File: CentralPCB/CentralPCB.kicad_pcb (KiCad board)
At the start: 2 copper layers, 71.1 x 76.2 mm, 60 parts, among them J1 POWER HEADER, J2 SPI Header, J3 Conn_01x24, J4 Conn_01x24, J5 Conn_02x16_Odd_Even, J6 Conn_Coaxial, J7 Conn_02x10_Odd_Even, J8 Conn_01x05, U1 AD8531, U2 Teensy4.1, U3 BA7810CP-E2

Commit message: Finished CentralPCB
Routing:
- net GND: track 94.7 -> 103.7 mm, vias 19 -> 22
- net +5V: track 210.8 -> 213.4 mm
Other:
- board size 71.1 x 76.2 mm -> 71.1 x 78.7 mm
- rule via_min_drill: 0.254 -> 0.3
- rule via_min_size: 0.508 -> 0.6
- board text added: "+12V"
- board text added: "+5V"
- board text added: "-12V"
- board text added: "12V"
- board text added: "3.3V"
- board text added: "5V"
- board text added: "AGND"
- board text added: "CS"
- board text added: "DAC POW"
- board text added: "DAC REF"
- board text added: "DAC SIG"
- board text added: "DGND"
- board text added: "DIN"
- board text added: "DVCC"
- board text added: "GND"
- board text added: "GND->"
- board text added: "MISO"
- board text added: "MOSI"
- board text added: "MREC"
- board text added: "MTRA"
- board text added: "SCK"
- board text added: "SCL"
- board text added: "SCLK"
- board text added: "SDA"
- board text added: "SPI"
- board text added: "VDD"
- board text added: "VSS"

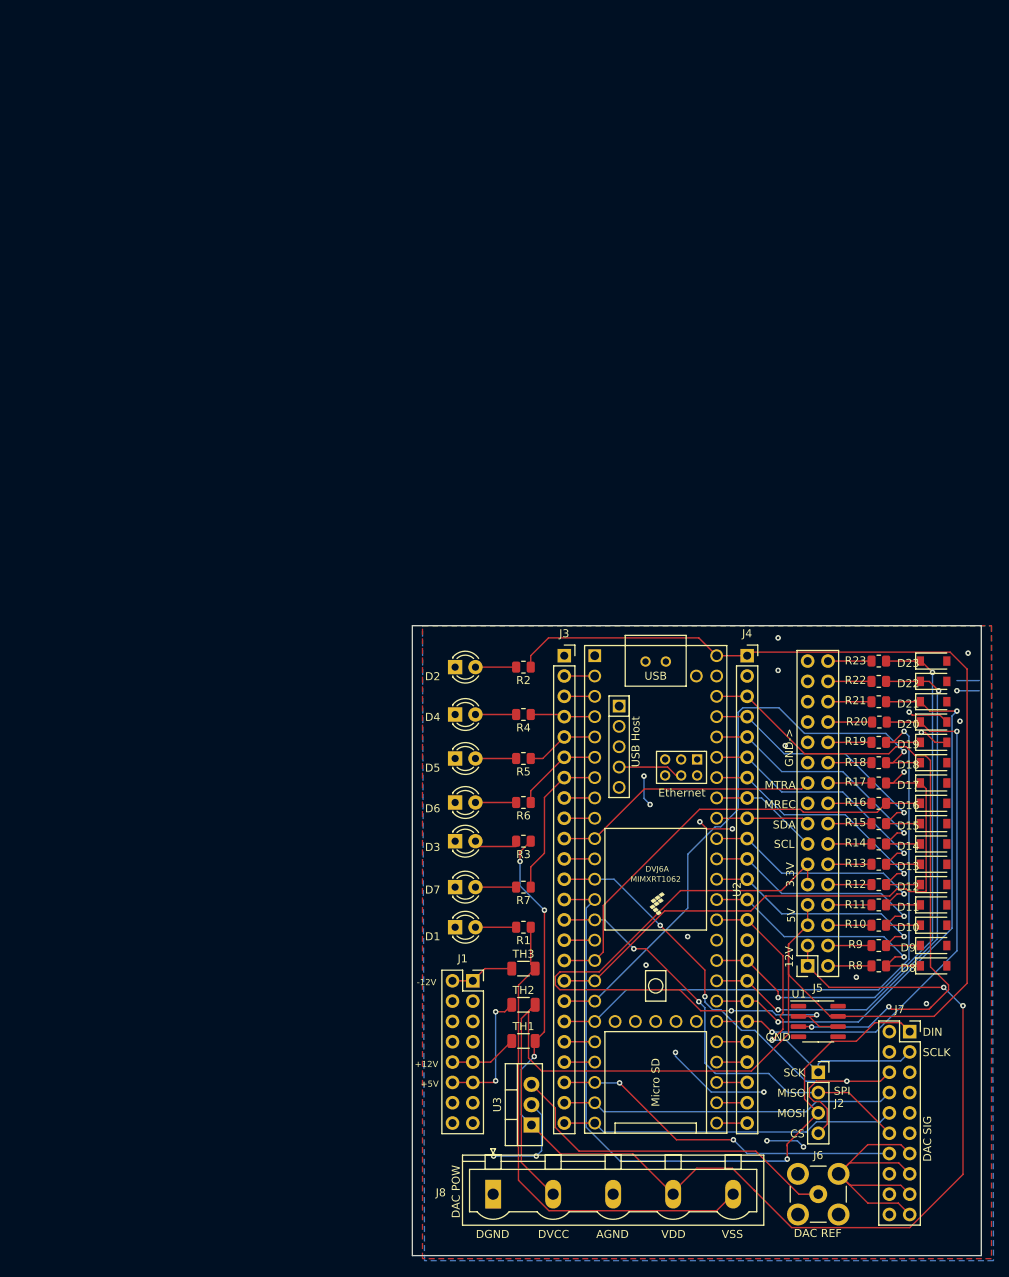
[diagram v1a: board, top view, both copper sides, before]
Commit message: Added additional protection for CentralPCB
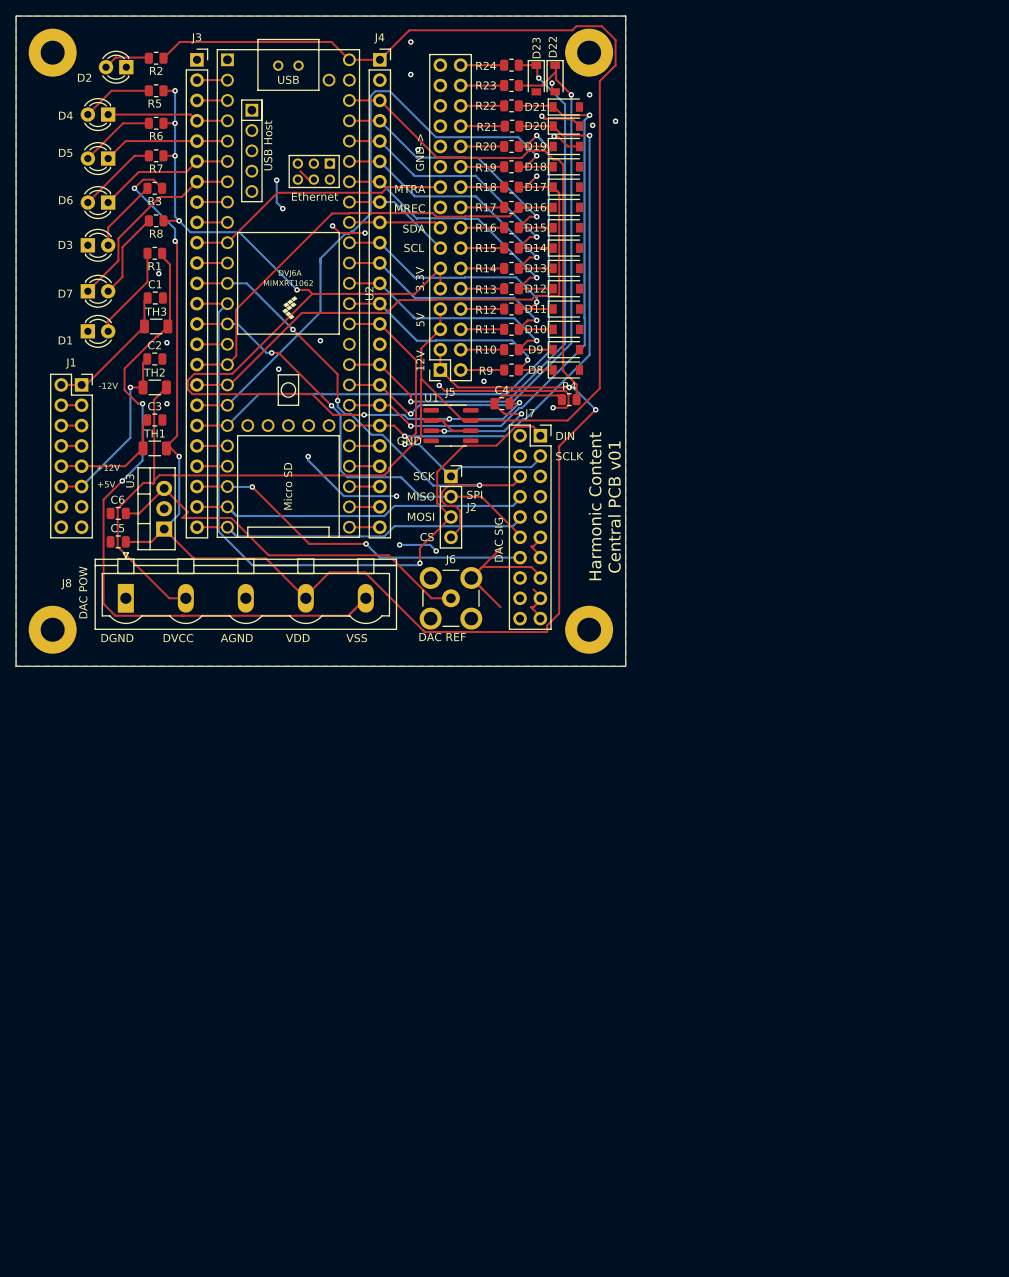
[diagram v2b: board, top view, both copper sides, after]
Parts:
- added  : MountingHole_3mm_Pad, MountingHole:MountingHole_3mm_Pad, F.Cu at (97.0, 102.1)
- added  : MountingHole_3mm_Pad, MountingHole:MountingHole_3mm_Pad, F.Cu at (30.0, 102.1)
- added  : MountingHole_3mm_Pad, MountingHole:MountingHole_3mm_Pad, F.Cu at (30.0, 30.0)
- added  : MountingHole_3mm_Pad, MountingHole:MountingHole_3mm_Pad, F.Cu at (97.0, 30.0)
- added C1: .1u, Capacitor_SMD:C_0805_2012Metric, F.Cu at (42.8, 60.6)
- added C2: .1u, Capacitor_SMD:C_0805_2012Metric, F.Cu at (42.7, 68.3)
- added C3: .1u, Capacitor_SMD:C_0805_2012Metric, F.Cu at (42.7, 75.9)
- added C4: .1u, Capacitor_SMD:C_0805_2012Metric, F.Cu at (86.1, 73.9)
- added C5: .33u, Capacitor_SMD:C_0805_2012Metric, F.Cu at (38.2, 91.1)
- added C6: .1u, Capacitor_SMD:C_0805_2012Metric, F.Cu at (38.2, 87.6)
- added R4: 10k, Resistor_SMD:R_0805_2012Metric, F.Cu at (94.6, 73.3)
- moved R1 96.0 mm to (42.7, 55.1)
- moved R8 95.1 mm to (42.9, 51.0)
- moved R3 93.7 mm to (42.7, 46.9)
- moved R7 93.0 mm to (42.9, 42.9)
- moved TH3 92.5 mm to (42.9, 64.2)
- moved R6 91.7 mm to (42.9, 38.8)
- moved R5 90.5 mm to (42.9, 34.7)
- moved TH2 89.9 mm to (42.7, 71.8)
- moved J1 89.1 mm to (33.6, 71.5)
- moved D22 89.0 mm to (92.8, 33.2), turned to 270 degrees
- moved R2 88.9 mm to (42.9, 30.7)
- moved D23 88.1 mm to (90.4, 33.2), turned to 270 degrees
- moved J7 87.6 mm to (90.9, 77.9)
- moved D10 87.5 mm to (94.2, 64.6)
- moved D11 87.5 mm to (94.2, 62.0)
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- renumbered R9 to R10, R10 to R11, R11 to R12, R12 to R13, R13 to R14, R14 to R15, R15 to R16, R16 to R17, R17 to R18, R18 to R19, R19 to R20, R20 to R21, R21 to R22, R22 to R23, R23 to R24, R4 to R5, R5 to R6, R6 to R7, R7 to R8, R8 to R9
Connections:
- D4 pad 1: GND -> Net-(D4-Pad1)
- D5 pad 1: GND -> Net-(D5-Pad1)
- D6 pad 1: GND -> Net-(D6-Pad1)
- D7 pad 1: GND -> Net-(D7-Pad1)
- J3 pad 4: Net-(J3-Pad4) -> Net-(D4-Pad1)
- J3 pad 5: Net-(J3-Pad5) -> Net-(D5-Pad1)
- J3 pad 6: Net-(J3-Pad6) -> Net-(D6-Pad1)
- J3 pad 7: Net-(J3-Pad7) -> Net-(D7-Pad1)
- R5 pad 1: Net-(J3-Pad4) -> +3V3
- R6 pad 1: Net-(J3-Pad5) -> +3V3
- R7 pad 1: Net-(J3-Pad6) -> +3V3
- R8 pad 1: Net-(J3-Pad7) -> +3V3
- U1 pad 3: Net-(J4-Pad3) -> Net-(C4-Pad1)
- U2 pad 4: Net-(J3-Pad4) -> Net-(D4-Pad1)
- U2 pad 5: Net-(J3-Pad5) -> Net-(D5-Pad1)
- U2 pad 6: Net-(J3-Pad6) -> Net-(D6-Pad1)
- U2 pad 7: Net-(J3-Pad7) -> Net-(D7-Pad1)
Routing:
- net +3V3: track 83.0 -> 137.4 mm, vias 2 -> 8
- net Net-(C4-Pad1): track 0.00 -> 25.5 mm, vias 0 -> 2
- net -12V: track 62.0 -> 87.5 mm, vias 0 -> 2
- net Net-(D7-Pad1): track 0.00 -> 24.7 mm
- net Net-(J4-Pad3): track 81.6 -> 60.9 mm, vias 2 -> 0
- net Net-(J3-Pad7): track 19.2 -> 0.00 mm
- net +12V: track 149.2 -> 167.8 mm
- net Net-(D6-Pad1): track 0.00 -> 17.0 mm
- net Net-(D5-Pad1): track 0.00 -> 15.8 mm
- net Net-(D4-Pad1): track 0.00 -> 15.6 mm
- net Net-(J3-Pad6): track 11.2 -> 0.00 mm
- net Net-(J3-Pad5): track 9.11 -> 0.00 mm
- net Net-(C1-Pad1): track 8.04 -> 17.1 mm
- net Net-(J3-Pad4): track 8.11 -> 0.00 mm
- net +5V: track 213.4 -> 220.7 mm
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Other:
- board size 71.1 x 78.7 mm -> 76.2 x 81.3 mm
- net class Default: trace_width 0.1778 -> 0.254
- rule trace_min: 0.1524 -> 0.254
- board text added: "Harmonic Content Central PCB v01"

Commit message: small silkscreen changes on centralpcb
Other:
- board text added: "Eurorack power"
- board text added: "Red Stripe"
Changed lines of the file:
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@@
-(kicad_pcb (version 20171130) (host pcbnew "(5.1.10)-1")
+(kicad_pcb (version 20171130) (host pcbnew "(5.1.4)-1")
   (general
     (thickness 1.6)
-    (drawings 34)
+    (drawings 36)
     (tracks 680)
     (zones 0)
@@
     )
   )
+  (gr_text "Eurorack power" (at 27.9 80.4 90) (layer F.SilkS)
+    (effects (font (size 1 1) (thickness 0.15)))
+  )
+  (gr_text "Red Stripe" (at 35.9 68.9) (layer F.SilkS)
+    (effects (font (size 0.508 0.508) (thickness 0.127)))
+  )
   (dimension 76.2 (width 0.15) (layer Dwgs.User)
     (gr_text "3.0000 in" (at 63.5 22.83) (layer Dwgs.User)
@@
   (segment (start 94.964799 38.289799) (end 93.788799 38.289799) (width 0.254) (layer F.Cu) (net 2))
   (segment (start 90.072799 97.057799) (end 91.1895 98.1745) (width 0.254) (layer F.Cu) (net 2))
+  (via (at 92.3925 33.782) (size 0.6858) (drill 0.3302) (layers F.Cu B.Cu) (net 2))
+  (segment (start 92.3925 34.4795) (end 92.7735 34.8605) (width 0.254) (layer F.Cu) (net 2))
+  (segment (start 92.3925 33.782) (end 92.3925 34.4795) (width 0.254) (layer F.Cu) (net 2))
   (via (at 90.7415 33.147) (size 0.6858) (drill 0.3302) (layers F.Cu B.Cu) (net 3))
   (via (at 74.7395 73.5965) (size 0.6858) (drill 0.3302) (layers F.Cu B.Cu) (net 3))
@@
   (segment (start 74.7395 73.5965) (end 86.758736 73.5965) (width 0.254) (layer B.Cu) (net 3))
   (segment (start 88.3606 31.6611) (end 88.236 31.5365) (width 0.254) (layer F.Cu) (net 3))
+  (segment (start 90.527 31.5365) (end 90.551 31.5605) (width 0.254) (layer F.Cu) (net 3))
+  (segment (start 88.236 31.5365) (end 90.527 31.5365) (width 0.254) (layer F.Cu) (net 3))
+  (segment (start 90.551 32.9565) (end 90.7415 33.147) (width 0.254) (layer F.Cu) (net 3))
+  (segment (start 90.551 31.5605) (end 90.551 32.9565) (width 0.254) (layer F.Cu) (net 3))
+  (segment (start 94.020618 36.426118) (end 94.020618 66.334618) (width 0.254) (layer B.Cu) (net 3))
+  (segment (start 90.7415 33.147) (end 94.020618 36.426118) (width 0.254) (layer B.Cu) (net 3))
   (via (at 94.8055 35.2425) (size 0.6858) (drill 0.3302) (layers F.Cu B.Cu) (net 4))
   (via (at 74.7395 75.1205) (size 0.6858) (drill 0.3302) (layers F.Cu B.Cu) (net 4))
@@
   (segment (start 75.83169 74.02831) (end 87.065092 74.02831) (width 0.254) (layer B.Cu) (net 4))
   (segment (start 74.7395 75.1205) (end 75.83169 74.02831) (width 0.254) (layer B.Cu) (net 4))
+  (segment (start 92.9005 32.328) (end 92.9005 31.624) (width 0.254) (layer F.Cu) (net 4))
+  (segment (start 91.152 34.0765) (end 92.9005 32.328) (width 0.254) (layer F.Cu) (net 4))
+  (segment (start 88.236 34.0765) (end 91.152 34.0765) (width 0.254) (layer F.Cu) (net 4))
+  (segment (start 92.9005 33.3375) (end 94.8055 35.2425) (width 0.254) (layer F.Cu) (net 4))
+  (segment (start 92.9005 32.328) (end 92.9005 33.3375) (width 0.254) (layer F.Cu) (net 4))
   (via (at 97.0915 37.7825) (size 0.6858) (drill 0.3302) (layers F.Cu B.Cu) (net 5))
   (via (at 74.7395 76.6445) (size 0.6858) (drill 0.3302) (layers F.Cu B.Cu) (net 5))
@@
   (segment (start 44.980799 82.781201) (end 43.318819 82.781201) (width 0.254) (layer F.Cu) (net 25))
   (segment (start 45.175991 82.781201) (end 44.980799 82.781201) (width 0.254) (layer F.Cu) (net 25))
-  (via (at 92.3925 33.782) (size 0.6858) (drill 0.3302) (layers F.Cu B.Cu) (net 2))
-  (segment (start 92.3925 34.4795) (end 92.7735 34.8605) (width 0.254) (layer F.Cu) (net 2))
-  (segment (start 92.3925 33.782) (end 92.3925 34.4795) (width 0.254) (layer F.Cu) (net 2))
-  (segment (start 90.527 31.5365) (end 90.551 31.5605) (width 0.254) (layer F.Cu) (net 3))
-  (segment (start 88.236 31.5365) (end 90.527 31.5365) (width 0.254) (layer F.Cu) (net 3))
-  (segment (start 90.551 32.9565) (end 90.7415 33.147) (width 0.254) (layer F.Cu) (net 3))
-  (segment (start 90.551 31.5605) (end 90.551 32.9565) (width 0.254) (layer F.Cu) (net 3))
-  (segment (start 94.020618 36.426118) (end 94.020618 66.334618) (width 0.254) (layer B.Cu) (net 3))
-  (segment (start 90.7415 33.147) (end 94.020618 36.426118) (width 0.254) (layer B.Cu) (net 3))
-  (segment (start 92.9005 32.328) (end 92.9005 31.624) (width 0.254) (layer F.Cu) (net 4))
-  (segment (start 91.152 34.0765) (end 92.9005 32.328) (width 0.254) (layer F.Cu) (net 4))
-  (segment (start 88.236 34.0765) (end 91.152 34.0765) (width 0.254) (layer F.Cu) (net 4))
-  (segment (start 92.9005 33.3375) (end 94.8055 35.2425) (width 0.254) (layer F.Cu) (net 4))
-  (segment (start 92.9005 32.328) (end 92.9005 33.3375) (width 0.254) (layer F.Cu) (net 4))
   (segment (start 70.8695 30.8645) (end 71.352301 30.381699) (width 0.254) (layer F.Cu) (net 25))
   (segment (start 74.558801 27.175199) (end 70.8695 30.8645) (width 0.254) (layer F.Cu) (net 25))
